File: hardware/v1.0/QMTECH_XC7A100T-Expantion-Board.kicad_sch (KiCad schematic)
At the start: 47 parts, among them J1 Micro_SD_Card_Det1, J14 USB_C_Receptacle_USB2.0_16P, J15 Conn_02x06_Odd_Even, J16 Conn_02x06_Odd_Even, J2 Conn_01x34, J3 USB_C_Receptacle_USB2.0_16P, J4 Conn_01x34, Q1 Si7121DN, U14 HUSB238, U15 CH340C

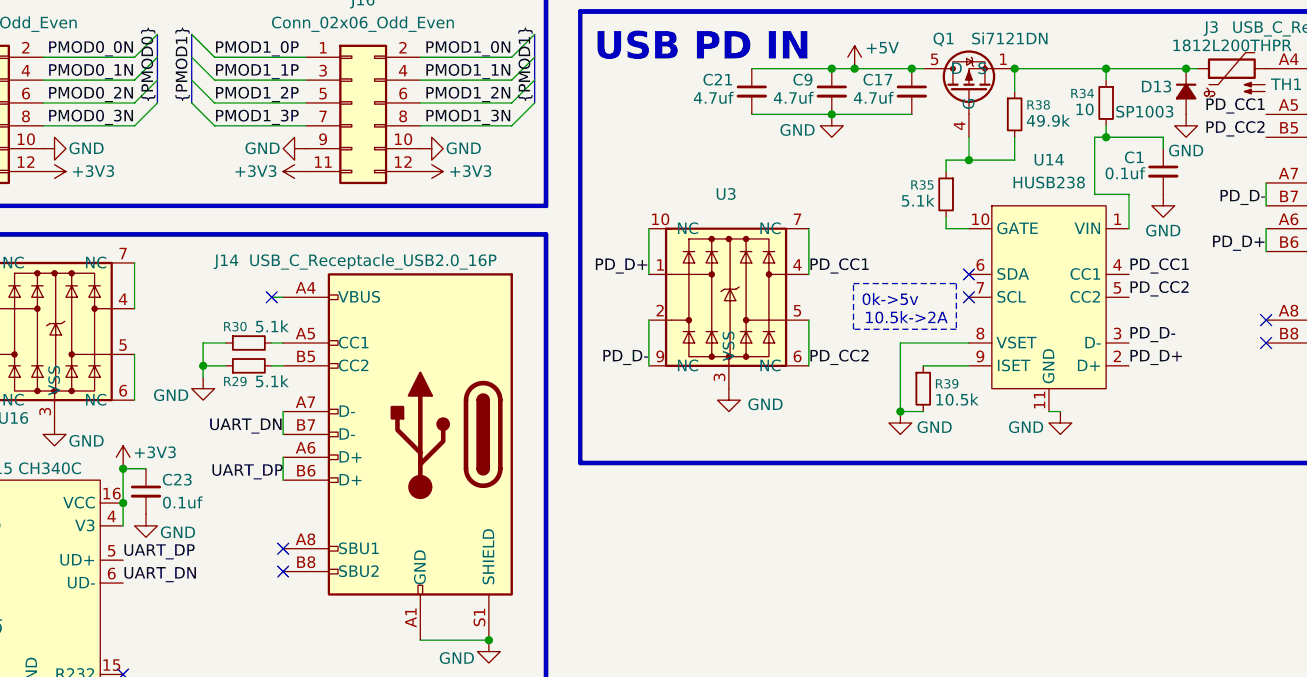
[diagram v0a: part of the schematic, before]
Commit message: added tvs diode+changed inductors
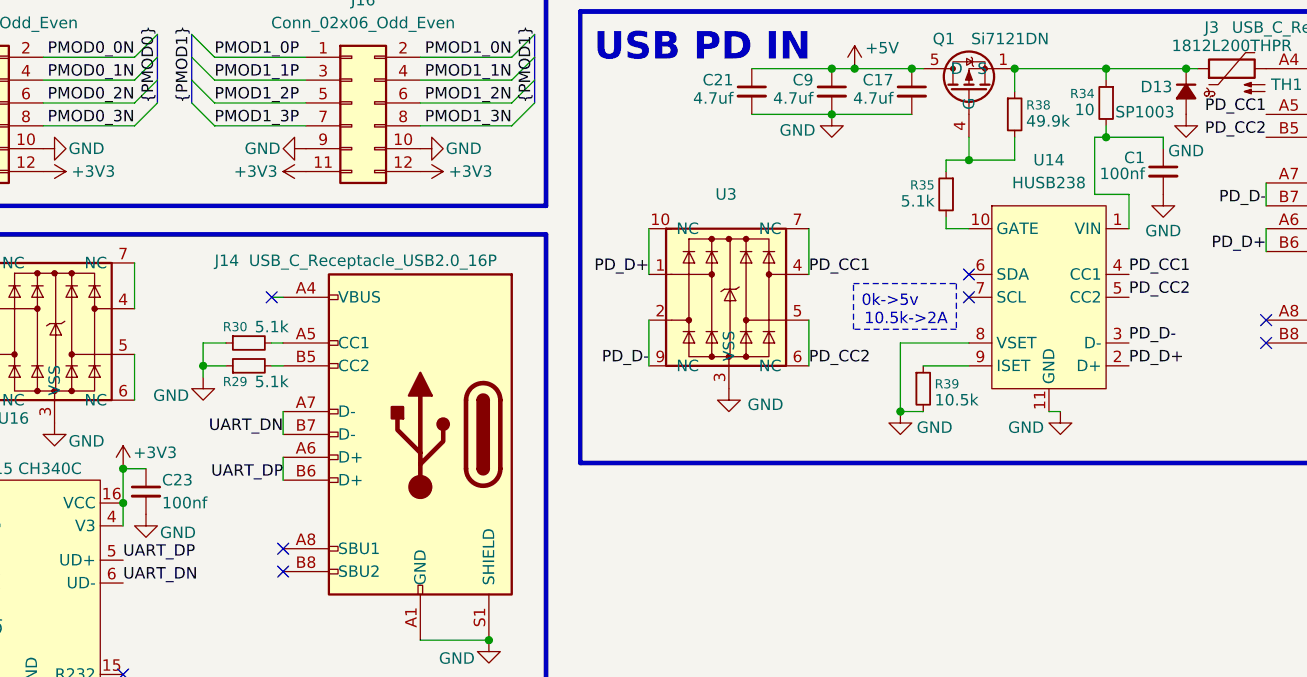
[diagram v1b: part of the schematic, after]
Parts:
- C1, C23: value 0.1uf -> 100nf
- D13: footprint (none) -> mylib:sod-723
- R1, R2, R28, R3, R4, R5, R6, R7: footprint Resistor_SMD:R_0603_1608Metric_Pad0.98x0.95mm_HandSolder -> Resistor_SMD:R_0603_1608Metric
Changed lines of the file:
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@@
 			)
 		)
-		(property "Footprint" "Resistor_SMD:R_0603_1608Metric_Pad0.98x0.95mm_HandSolder"
+		(property "Footprint" "Resistor_SMD:R_0603_1608Metric"
 			(at 26.67 135.89 0)
 			(effects
@@
 			)
 		)
-		(property "Value" "0.1uf"
+		(property "Value" "100nf"
 			(at 241.808 132.334 0)
 			(effects
@@
 			)
 		)
-		(property "Footprint" "Resistor_SMD:R_0603_1608Metric_Pad0.98x0.95mm_HandSolder"
+		(property "Footprint" "Resistor_SMD:R_0603_1608Metric"
 			(at 26.67 125.73 0)
 			(effects
@@
 			)
 		)
-		(property "Footprint" "Resistor_SMD:R_0603_1608Metric_Pad0.98x0.95mm_HandSolder"
+		(property "Footprint" "Resistor_SMD:R_0603_1608Metric"
 			(at 26.67 123.19 0)
 			(effects
@@
 			)
 		)
-		(property "Footprint" "Resistor_SMD:R_0603_1608Metric_Pad0.98x0.95mm_HandSolder"
+		(property "Footprint" "Resistor_SMD:R_0603_1608Metric"
 			(at 26.67 143.51 0)
 			(effects
@@
 			)
 		)
-		(property "Footprint" "Resistor_SMD:R_0603_1608Metric_Pad0.98x0.95mm_HandSolder"
+		(property "Footprint" "Resistor_SMD:R_0603_1608Metric"
 			(at 91.44 161.29 0)
 			(effects
@@
 			)
 		)
-		(property "Footprint" ""
+		(property "Footprint" "mylib:sod-723"
 			(at 246.38 123.19 90)
 			(effects
@@
 			)
 		)
-		(property "Footprint" "Resistor_SMD:R_0603_1608Metric_Pad0.98x0.95mm_HandSolder"
+		(property "Footprint" "Resistor_SMD:R_0603_1608Metric"
 			(at 26.67 120.65 0)
 			(effects
@@
 			)
 		)
-		(property "Value" "0.1uf"
+		(property "Value" "100nf"
 			(at 132.588 168.91 0)
 			(effects
@@
 			)
 		)
-		(property "Footprint" "Resistor_SMD:R_0603_1608Metric_Pad0.98x0.95mm_HandSolder"
+		(property "Footprint" "Resistor_SMD:R_0603_1608Metric"
 			(at 26.67 138.43 0)
 			(effects
@@
 			)
 		)
-		(property "Footprint" "Resistor_SMD:R_0603_1608Metric_Pad0.98x0.95mm_HandSolder"
+		(property "Footprint" "Resistor_SMD:R_0603_1608Metric"
 			(at 26.67 130.81 0)
 			(effects
